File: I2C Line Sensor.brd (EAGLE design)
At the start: 63.5 x 12.1 mm, 31 parts, among them U1 ADS7830

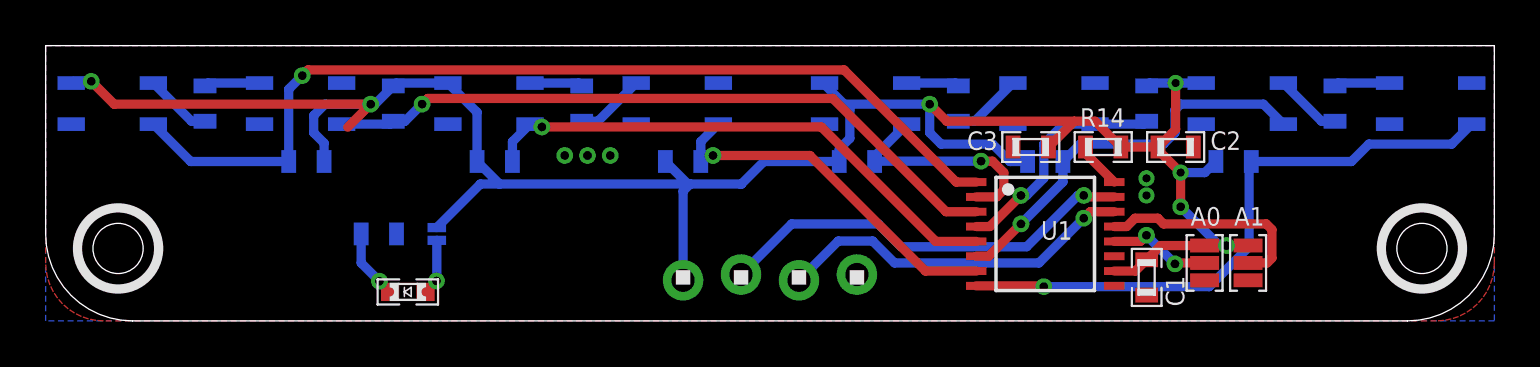
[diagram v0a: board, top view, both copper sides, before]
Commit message: Cleaned up layout of I2C Mini Line Sensor and I2C Line Sensor Also geenerated preview images
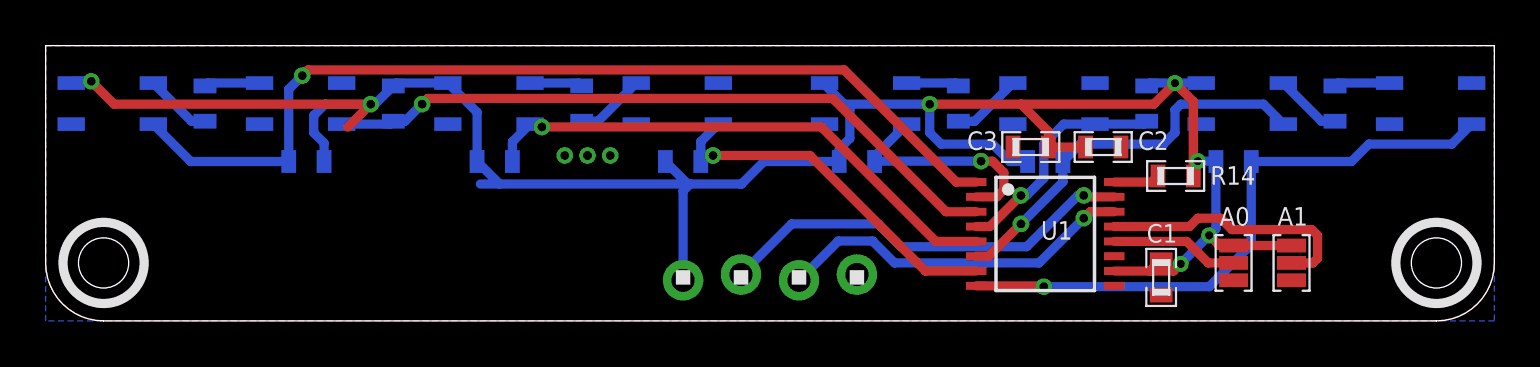
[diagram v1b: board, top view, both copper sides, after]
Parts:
- removed J1: (no value), .solderjumper:2.MED
- removed LED1: (no value), standardparts:0603.LED
- removed R13: 1k, standardparts:0603
- moved R14 3.42 mm to (49.5, 6.35)
- moved C2 3.18 mm to (46.4, 7.62)
- moved A1 1.91 mm to (54.6, 2.54)
- moved A0 1.27 mm to (52.1, 2.54)
- moved C1 0.64 mm to (48.9, 1.91)
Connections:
- removed net N$11: LED1.P$2, R13.2
- removed net N$12: J1.1, LED1.P$1
- net 3.3V: no longer J1.2
- net GND: no longer R13.1
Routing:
- net N$11: track 3.07 -> 0.00 mm, vias 1 -> 0
- net N$12: track 2.47 -> 0.00 mm, vias 1 -> 0
- net N$10: track 9.65 -> 11.6 mm
- net 3.3V: track 99.3 -> 100.7 mm
- net N$1: track 4.60 -> 5.62 mm, vias 2 -> 0
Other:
- outline, holes or cut-outs redrawn
- board text removed: "PWR On"

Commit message: Regenerate screnshots
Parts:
- R13: value 5 -> 5.1
- renumbered R14 to R13
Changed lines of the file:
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@@
 <setting verticaltext="up"/>
 </settings>
-<grid distance="0.25" unitdist="mm" unit="mm" style="dots" multiple="2" display="yes" altdistance="0.05" altunitdist="mm" altunit="mm"/>
+<grid distance="25" unitdist="mil" unit="mil" style="dots" multiple="2" display="yes" altdistance="5" altunitdist="mil" altunit="mil"/>
 <layers>
 <layer number="1" name="Top" color="4" fill="1" visible="yes" active="yes"/>
@@
 <text x="47.625" y="0.635" size="1.016" layer="52" ratio="12" rot="MR0" align="bottom-center">Cruz Monrreal II</text>
 <text x="15.875" y="0.635" size="1.016" layer="52" ratio="12" rot="MR0" align="bottom-center">AnomalousMaker.com</text>
-<text x="15.875" y="1.27" size="1.6764" layer="51" ratio="12" align="bottom-center">I2C Line Sensor</text>
+<text x="15.875" y="1.905" size="1.6764" layer="51" ratio="12" align="bottom-center">I2C Line
+Sensor</text>
 <text x="27.94" y="3.175" size="0.8128" layer="52" font="vector" ratio="12" rot="MR90" align="center-left">VCC</text>
 <text x="30.48" y="3.175" size="0.8128" layer="52" font="vector" ratio="12" rot="MR90" align="center-left">SDA</text>
@@
 <element name="U$8" library="SparkFun" package="QRE1113" value="QRE1113" x="60.706" y="9.525" smashed="yes" rot="MR180"/>
 <element name="U1" library="burr-brown" package="TSSOP16-PW" value="ADS7830" x="43.815" y="3.81" smashed="yes" rot="R270">
-<attribute name="NAME" x="43.628" y="3.56" size="0.8128" layer="25" ratio="12"/>
+<attribute name="NAME" x="43.12" y="3.306" size="0.8128" layer="25" ratio="12"/>
 </element>
 <element name="R1" library="standardparts" package="0603" value="33" x="6.985" y="9.525" smashed="yes" rot="MR270">
@@
 </element>
 <element name="U$11" library="headers(.1in)" package="1X4.LOCK" value="1X4.LOCK" x="27.94" y="1.905"/>
-<element name="R14" library="standardparts" package="0603" value="5" x="49.53" y="6.35" smashed="yes">
+<element name="R13" library="standardparts" package="0603" value="5.1" x="49.53" y="6.35" smashed="yes">
 <attribute name="NAME" x="51.054" y="5.969" size="0.8128" layer="25" font="vector" ratio="12"/>
 </element>
@@
 <wire x1="13.24" y1="8.49" x2="14.25" y2="9.5" width="0.4064" layer="1"/>
 <contactref element="U$11" pad="1"/>
-<contactref element="R14" pad="2"/>
+<contactref element="R13" pad="2"/>
 <contactref element="C3" pad="2"/>
 <contactref element="C2" pad="2"/>
@@
 <signal name="N$15">
 <contactref element="U1" pad="16"/>
-<contactref element="R14" pad="1"/>
+<contactref element="R13" pad="1"/>
 <wire x1="46.84" y1="6.085" x2="48.49" y2="6.085" width="0.4064" layer="1"/>
 <wire x1="48.49" y1="6.085" x2="48.755" y2="6.35" width="0.4064" layer="1"/>
@@
 </board>
 </drawing>
+<compatibility>
+<note version="6.3" minversion="6.2.2" severity="warning">
+Since Version 6.2.2 text objects can contain more than one line,
+which will not be processed correctly with this version.
+</note>
+</compatibility>
 </eagle>

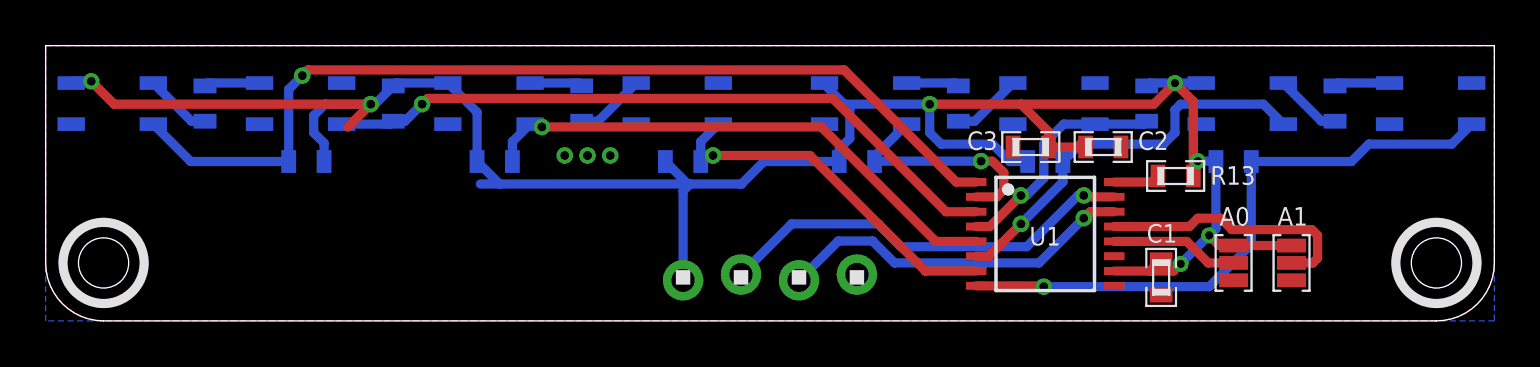
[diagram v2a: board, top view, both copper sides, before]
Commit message: Minor Updates to I2CLine Sensor Removed header labeling on bottom layer and spaced resistors away from IR sensors
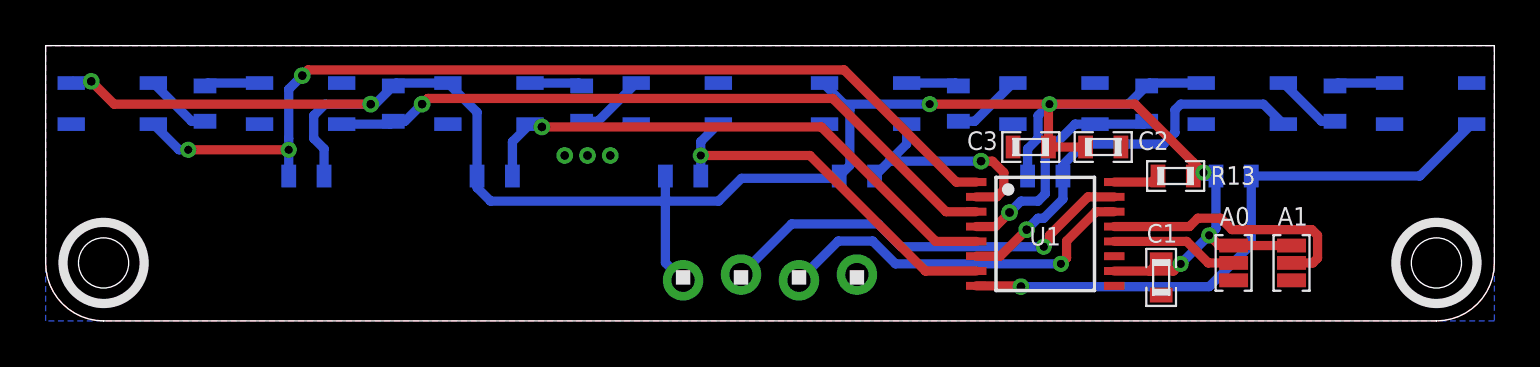
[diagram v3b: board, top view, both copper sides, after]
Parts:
- moved R10 0.64 mm to (27.9, 6.35)
- moved R12 0.64 mm to (52.1, 6.35)
- moved R5 0.64 mm to (11.4, 6.35)
- moved R6 0.64 mm to (19.7, 6.35)
- moved R7 0.64 mm to (35.6, 6.35)
- moved R8 0.64 mm to (43.8, 6.35)
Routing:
- net 3.3V: track 100.7 -> 98.8 mm
- net C: track 23.6 -> 24.3 mm
- net D: track 16.2 -> 16.8 mm
- net H: track 26.9 -> 26.4 mm
- net A: track 42.3 -> 42.7 mm, vias 1 -> 3

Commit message: Changd R[1-4] values to 51 ohms instead of 33 ohms. PCBs should no longer heat up due to current draw.
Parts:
- R1, R2, R3, R4: value 33 -> 51
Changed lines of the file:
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@@
 <setting verticaltext="up"/>
 </settings>
-<grid distance="0.25" unitdist="mm" unit="mm" style="dots" multiple="2" display="yes" altdistance="0.05" altunitdist="mm" altunit="mm"/>
+<grid distance="25" unitdist="mil" unit="mil" style="dots" multiple="2" display="yes" altdistance="5" altunitdist="mil" altunit="mil"/>
 <layers>
 <layer number="1" name="Top" color="4" fill="1" visible="yes" active="yes"/>
@@
 <attribute name="NAME" x="43.12" y="3.306" size="0.8128" layer="25" ratio="12"/>
 </element>
-<element name="R1" library="standardparts" package="0603" value="33" x="6.985" y="9.525" smashed="yes" rot="MR270">
+<element name="R1" library="standardparts" package="0603" value="51" x="6.985" y="9.525" smashed="yes" rot="MR270">
 <attribute name="NAME" x="7.62" y="7.112" size="0.8128" layer="26" font="vector" ratio="12" rot="MR0"/>
 </element>
-<element name="R2" library="standardparts" package="0603" value="33" x="23.495" y="9.525" smashed="yes" rot="MR90">
+<element name="R2" library="standardparts" package="0603" value="51" x="23.495" y="9.525" smashed="yes" rot="MR90">
 <attribute name="NAME" x="24.13" y="7.112" size="0.8128" layer="26" font="vector" ratio="12" rot="MR0"/>
 </element>
-<element name="R3" library="standardparts" package="0603" value="33" x="40.005" y="9.525" smashed="yes" rot="MR90">
+<element name="R3" library="standardparts" package="0603" value="51" x="40.005" y="9.525" smashed="yes" rot="MR90">
 <attribute name="NAME" x="40.513" y="7.112" size="0.8128" layer="26" font="vector" ratio="12" rot="MR0"/>
 </element>
-<element name="R4" library="standardparts" package="0603" value="33" x="56.515" y="9.525" smashed="yes" rot="MR270">
+<element name="R4" library="standardparts" package="0603" value="51" x="56.515" y="9.525" smashed="yes" rot="MR270">
 <attribute name="NAME" x="57.15" y="7.112" size="0.8128" layer="26" font="vector" ratio="12" rot="MR0"/>
 </element>

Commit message: Modified resistor values such that the PCBs should no longer get hot
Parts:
- renumbered U$1 to U2, U$2 to U3, U$3 to U4, U$4 to U5, U$5 to U6, U$6 to U7, U$7 to U8, U$8 to U9
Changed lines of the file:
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@@
 </autorouter>
 <elements>
-<element name="U$1" library="SparkFun" package="QRE1113" value="QRE1113" x="2.921" y="9.525" smashed="yes" rot="MR180"/>
-<element name="U$2" library="SparkFun" package="QRE1113" value="QRE1113" x="11.176" y="9.525" smashed="yes" rot="MR180"/>
-<element name="U$3" library="SparkFun" package="QRE1113" value="QRE1113" x="19.431" y="9.525" smashed="yes" rot="MR180"/>
-<element name="U$4" library="SparkFun" package="QRE1113" value="QRE1113" x="27.686" y="9.525" smashed="yes" rot="MR180"/>
-<element name="U$5" library="SparkFun" package="QRE1113" value="QRE1113" x="35.941" y="9.525" smashed="yes" rot="MR180"/>
-<element name="U$6" library="SparkFun" package="QRE1113" value="QRE1113" x="44.196" y="9.525" smashed="yes" rot="MR180"/>
-<element name="U$7" library="SparkFun" package="QRE1113" value="QRE1113" x="52.451" y="9.525" smashed="yes" rot="MR180"/>
-<element name="U$8" library="SparkFun" package="QRE1113" value="QRE1113" x="60.706" y="9.525" smashed="yes" rot="MR180"/>
+<element name="U2" library="SparkFun" package="QRE1113" value="QRE1113" x="2.921" y="9.525" smashed="yes" rot="MR180"/>
+<element name="U3" library="SparkFun" package="QRE1113" value="QRE1113" x="11.176" y="9.525" smashed="yes" rot="MR180"/>
+<element name="U4" library="SparkFun" package="QRE1113" value="QRE1113" x="19.431" y="9.525" smashed="yes" rot="MR180"/>
+<element name="U5" library="SparkFun" package="QRE1113" value="QRE1113" x="27.686" y="9.525" smashed="yes" rot="MR180"/>
+<element name="U6" library="SparkFun" package="QRE1113" value="QRE1113" x="35.941" y="9.525" smashed="yes" rot="MR180"/>
+<element name="U7" library="SparkFun" package="QRE1113" value="QRE1113" x="44.196" y="9.525" smashed="yes" rot="MR180"/>
+<element name="U8" library="SparkFun" package="QRE1113" value="QRE1113" x="52.451" y="9.525" smashed="yes" rot="MR180"/>
+<element name="U9" library="SparkFun" package="QRE1113" value="QRE1113" x="60.706" y="9.525" smashed="yes" rot="MR180"/>
 <element name="U1" library="burr-brown" package="TSSOP16-PW" value="ADS7830" x="43.815" y="3.81" smashed="yes" rot="R270">
 <attribute name="NAME" x="43.12" y="3.306" size="0.8128" layer="25" ratio="12"/>
@@
 <vertex x="0" y="0"/>
 </polygon>
-<contactref element="U$2" pad="2"/>
-<contactref element="U$8" pad="2"/>
-<contactref element="U$4" pad="2"/>
-<contactref element="U$6" pad="2"/>
-<contactref element="U$4" pad="4"/>
-<contactref element="U$6" pad="4"/>
-<contactref element="U$2" pad="4"/>
-<contactref element="U$8" pad="4"/>
-<contactref element="U$1" pad="4"/>
-<contactref element="U$5" pad="4"/>
-<contactref element="U$3" pad="4"/>
-<contactref element="U$7" pad="4"/>
+<contactref element="U3" pad="2"/>
+<contactref element="U9" pad="2"/>
+<contactref element="U5" pad="2"/>
+<contactref element="U7" pad="2"/>
+<contactref element="U5" pad="4"/>
+<contactref element="U7" pad="4"/>
+<contactref element="U3" pad="4"/>
+<contactref element="U9" pad="4"/>
+<contactref element="U2" pad="4"/>
+<contactref element="U6" pad="4"/>
+<contactref element="U4" pad="4"/>
+<contactref element="U8" pad="4"/>
 <contactref element="U1" pad="9"/>
 <contactref element="A1" pad="3"/>
@@
 </signal>
 <signal name="N$2">
-<contactref element="U$1" pad="2"/>
+<contactref element="U2" pad="2"/>
 <contactref element="R1" pad="2"/>
 <wire x1="4.721" y1="10.425" x2="6.396" y2="8.75" width="0.4064" layer="16"/>
@@
 </signal>
 <signal name="N$3">
-<contactref element="U$2" pad="1"/>
+<contactref element="U3" pad="1"/>
 <contactref element="R1" pad="1"/>
 <wire x1="6.985" y1="10.3" x2="7.11" y2="10.425" width="0.4064" layer="16"/>
@@
 </signal>
 <signal name="N$4">
-<contactref element="U$4" pad="1"/>
+<contactref element="U5" pad="1"/>
 <contactref element="R2" pad="1"/>
 <wire x1="25.886" y1="10.425" x2="24.211" y2="8.75" width="0.4064" layer="16"/>
@@
 </signal>
 <signal name="N$5">
-<contactref element="U$3" pad="2"/>
+<contactref element="U4" pad="2"/>
 <contactref element="R2" pad="2"/>
 <wire x1="23.495" y1="10.3" x2="23.37" y2="10.425" width="0.4064" layer="16"/>
@@
 </signal>
 <signal name="N$6">
-<contactref element="U$5" pad="2"/>
+<contactref element="U6" pad="2"/>
 <contactref element="R3" pad="2"/>
 <wire x1="40.005" y1="10.3" x2="39.88" y2="10.425" width="0.4064" layer="16"/>
@@
 </signal>
 <signal name="N$7">
-<contactref element="U$6" pad="1"/>
+<contactref element="U7" pad="1"/>
 <contactref element="R3" pad="1"/>
 <wire x1="42.396" y1="10.425" x2="40.721" y2="8.75" width="0.4064" layer="16"/>
@@
 </signal>
 <signal name="N$8">
-<contactref element="U$7" pad="2"/>
+<contactref element="U8" pad="2"/>
 <contactref element="R4" pad="2"/>
 <wire x1="54.251" y1="10.425" x2="55.926" y2="8.75" width="0.4064" layer="16"/>
@@
 </signal>
 <signal name="N$9">
-<contactref element="U$8" pad="1"/>
+<contactref element="U9" pad="1"/>
 <contactref element="R4" pad="1"/>
 <wire x1="56.515" y1="10.3" x2="56.64" y2="10.425" width="0.4064" layer="16"/>
@@
 </signal>
 <signal name="A">
-<contactref element="U$1" pad="3"/>
+<contactref element="U2" pad="3"/>
 <contactref element="U1" pad="1"/>
 <contactref element="R5" pad="1"/>
@@
 </signal>
 <signal name="B">
-<contactref element="U$2" pad="3"/>
+<contactref element="U3" pad="3"/>
 <contactref element="U1" pad="3"/>
 <contactref element="R9" pad="1"/>
@@
 </signal>
 <signal name="C">
-<contactref element="U$3" pad="3"/>
+<contactref element="U4" pad="3"/>
 <contactref element="U1" pad="5"/>
 <contactref element="R6" pad="1"/>
@@
 </signal>
 <signal name="D">
-<contactref element="U$4" pad="3"/>
+<contactref element="U5" pad="3"/>
 <contactref element="U1" pad="7"/>
 <contactref element="R10" pad="1"/>
@@
 </signal>
 <signal name="E">
-<contactref element="U$5" pad="3"/>
+<contactref element="U6" pad="3"/>
 <contactref element="U1" pad="2"/>
 <contactref element="R7" pad="1"/>
@@
 </signal>
 <signal name="F">
-<contactref element="U$6" pad="3"/>
+<contactref element="U7" pad="3"/>
 <contactref element="U1" pad="4"/>
 <contactref element="R11" pad="1"/>
@@
 </signal>
 <signal name="G">
-<contactref element="U$7" pad="3"/>
+<contactref element="U8" pad="3"/>
 <contactref element="U1" pad="6"/>
 <contactref element="R8" pad="1"/>
@@
 </signal>
 <signal name="H">
-<contactref element="U$8" pad="3"/>
+<contactref element="U9" pad="3"/>
 <contactref element="U1" pad="8"/>
 <contactref element="R12" pad="1"/>
@@
 <signal name="3.3V">
 <contactref element="U1" pad="10"/>
-<contactref element="U$1" pad="1"/>
-<contactref element="U$3" pad="1"/>
-<contactref element="U$5" pad="1"/>
-<contactref element="U$7" pad="1"/>
+<contactref element="U2" pad="1"/>
+<contactref element="U4" pad="1"/>
+<contactref element="U6" pad="1"/>
+<contactref element="U8" pad="1"/>
 <contactref element="R5" pad="2"/>
 <contactref element="R6" pad="2"/>
